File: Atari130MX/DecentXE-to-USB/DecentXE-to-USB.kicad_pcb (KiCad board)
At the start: 2 copper layers, 50.5 x 62.7 mm, 21 parts, among them J1 Conn_01x26, J2 Conn_01x09, Q1 Q_NPN_EBC, U1 Pico

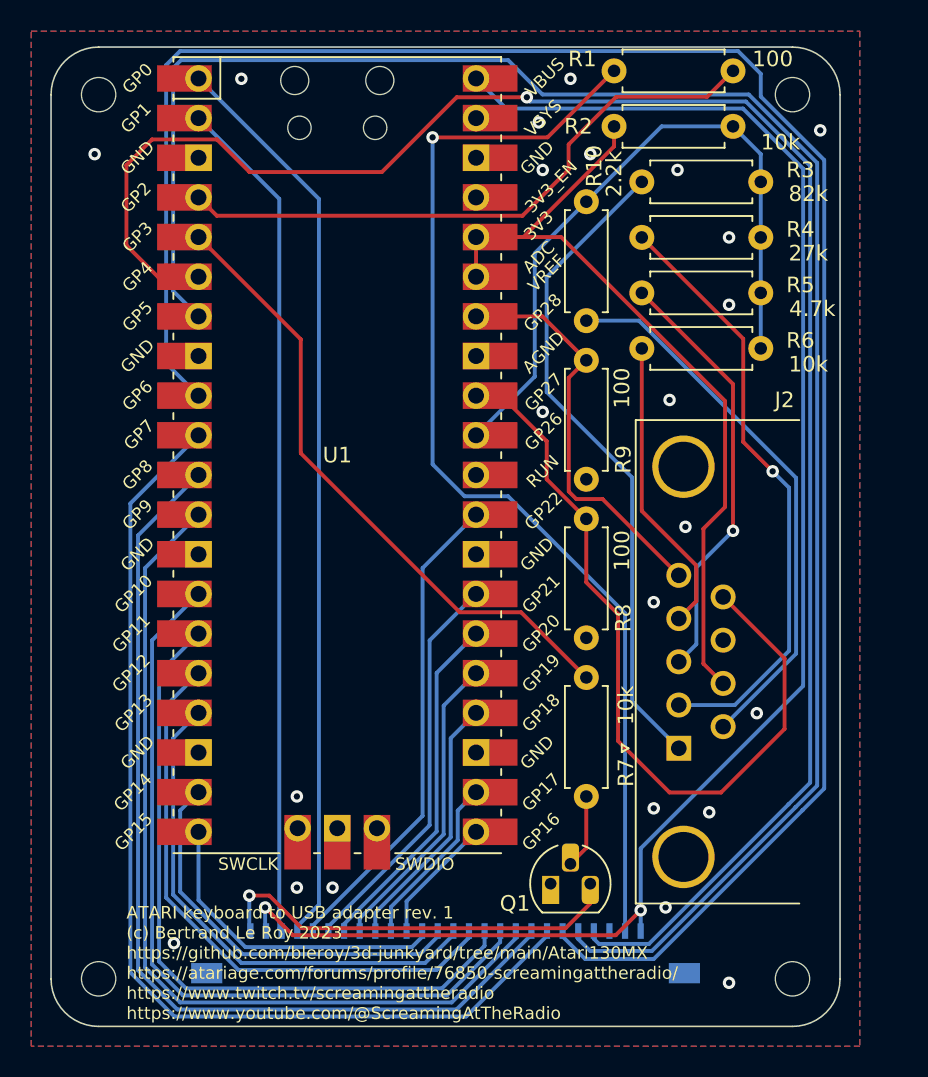
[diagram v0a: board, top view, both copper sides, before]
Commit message: Bettter design for the USB adapter
There will eventually be a 2040-based design that will do away with the Pico entirely. This is only a prototype.
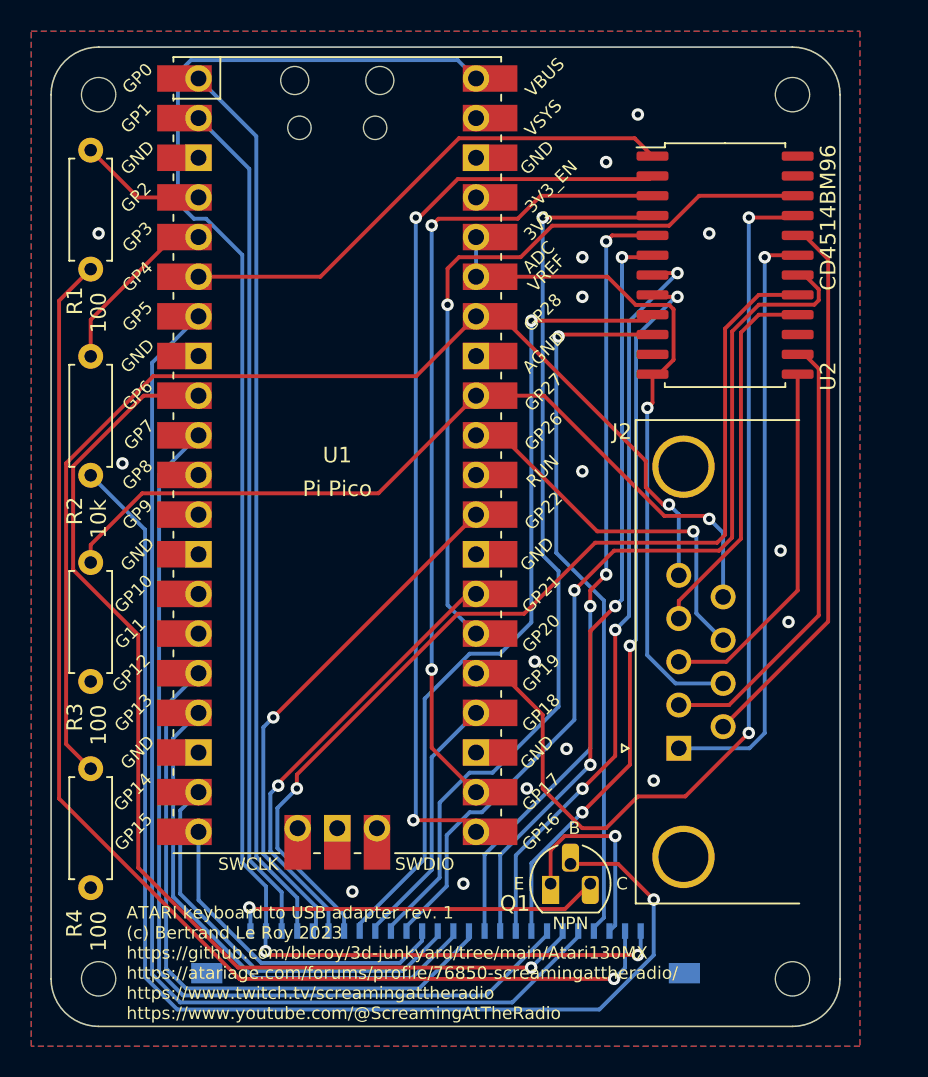
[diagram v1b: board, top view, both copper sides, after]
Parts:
- removed R10: 2.2k, Resistor_THT:R_Axial_DIN0207_L6.3mm_D2.5mm_P7.62mm_Horizontal
- removed R5: 4.7k, Resistor_THT:R_Axial_DIN0207_L6.3mm_D2.5mm_P7.62mm_Horizontal
- removed R6, R7: 10k, Resistor_THT:R_Axial_DIN0207_L6.3mm_D2.5mm_P7.62mm_Horizontal
- removed R8, R9: 100, Resistor_THT:R_Axial_DIN0207_L6.3mm_D2.5mm_P7.62mm_Horizontal
- removed REFe (x4): MountingHole_2.2mm_M2, MountingHole:MountingHole_2.2mm_M2
- added REF**: MountingHole_2.2mm_M2, MountingHole:MountingHole_2.2mm_M2, F.Cu at (15.7, 19.1)
- added REF**: MountingHole_2.2mm_M2, MountingHole:MountingHole_2.2mm_M2, F.Cu at (60.2, 19.1)
- added REF**: MountingHole_2.2mm_M2, MountingHole:MountingHole_2.2mm_M2, F.Cu at (60.2, 75.7)
- added REF**: MountingHole_2.2mm_M2, MountingHole:MountingHole_2.2mm_M2, F.Cu at (15.7, 75.7)
- added U2: CD4514BM96, Package_SO:SOIC-24W_7.5x15.4mm_P1.27mm, F.Cu at (55.9, 30.0)
- R3: value 82k -> 100
- R4: value 27k -> 100
- U1: value Pico -> Pi Pico
- moved R4 54.6 mm to (15.2, 69.8), turned to 90 degrees
- moved REF** 49.5 mm to (26.9, 29.5)
- moved R3 47.7 mm to (15.2, 56.6), turned to 90 degrees
- moved R2 40.3 mm to (15.2, 43.4), turned to 90 degrees
- moved R1 35.9 mm to (15.2, 30.2), turned to 90 degrees
- moved REF** 32.0 mm to (27.4, 40.1)
- moved G*** 2.29 mm to (27.6, 53.3)
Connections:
- J2 pad 8: GND -> JOY_GND
- R2 pad 1: 3V3 -> Net-(Q1-Pad2)
- R2 pad 2: Net-(U1-Pad31) -> Net-(R2-Pad2)
- R3 pad 1: UP -> GND
- R3 pad 2: Net-(U1-Pad31) -> PADDLE_A
- R4 pad 1: DOWN -> GND
- R4 pad 2: Net-(U1-Pad31) -> PADDLE_B
- U1 pad 11: COL_3 -> unconnected-(U1-Pad11)
- U1 pad 12: COL_4 -> unconnected-(U1-Pad12)
- U1 pad 14: COL_5 -> unconnected-(U1-Pad14)
- U1 pad 15: COL_6 -> unconnected-(U1-Pad15)
- U1 pad 21: COL_8 -> A0
- U1 pad 22: COL_7 -> A1
- U1 pad 25: COL_1 -> A2
- U1 pad 26: COL_9 -> A3
- U1 pad 31: Net-(U1-Pad31) -> JOY_GND
- U1 pad 5: Net-(R7-Pad2) -> Net-(R2-Pad2)
- U1 pad 6: COL_2 -> STROBE
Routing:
- net Net-(Q1-Pad2): track 4.74 -> 78.3 mm, vias 0 -> 1
- net COL_2: track 118.1 -> 45.5 mm
- net ROW_8: track 130.5 -> 68.0 mm, vias 0 -> 1
- net A2: track 0.00 -> 61.3 mm, vias 0 -> 2
- net A0: track 0.00 -> 59.3 mm, vias 0 -> 2
- net A1: track 0.00 -> 52.4 mm, vias 0 -> 2
- net COL_8: track 8.20 -> 59.5 mm, vias 0 -> 1
- net A3: track 0.00 -> 48.5 mm, vias 0 -> 1
- net ROW_7: track 121.2 -> 73.2 mm
- net COL_7: track 11.2 -> 58.0 mm, vias 0 -> 1
- net PADDLE_B: track 26.4 -> 71.9 mm, vias 0 -> 1
- net Net-(U1-Pad31): track 44.2 -> 0.00 mm
- net COL_9: track 22.6 -> 64.9 mm, vias 0 -> 1
- net Net-(R7-Pad2): track 40.8 -> 0.00 mm
- net STROBE: track 0.00 -> 33.2 mm
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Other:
- board text added: "B"
- board text added: "C"
- board text added: "E"
- board text added: "NPN"

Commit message: Fix the USB adapter
Decoder power supply was reversed. oops
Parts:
- U1: value Pi Pico -> Pico
- U2: value CD4514BM96 -> 4514
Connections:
- U2 pad 12: 3V3 -> GND
- U2 pad 24: GND -> 3V3
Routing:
- net 3V3: track 44.4 -> 61.6 mm, vias 1 -> 2

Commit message: USB adapter rev 2
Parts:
- removed Q1: Q_NPN_EBC, Package_TO_SOT_THT:TO-92_HandSolder
- removed R2: 10k, Resistor_THT:R_Axial_DIN0207_L6.3mm_D2.5mm_P7.62mm_Horizontal
- added R5: 100, Resistor_SMD:R_0603_1608Metric, B.Cu at (45.1, 50.2)
- added R6: 100, Resistor_SMD:R_0603_1608Metric, B.Cu at (45.1, 47.0)
- added R7: 100, Resistor_SMD:R_0603_1608Metric, B.Cu at (45.1, 40.6)
- added R8: 100, Resistor_SMD:R_0603_1608Metric, B.Cu at (45.1, 37.5)
- added R9: 100, Resistor_SMD:R_0603_1608Metric, B.Cu at (45.1, 43.8)
- G***, REF**: moved to F.Cu
- R1, R3, R4: footprint Resistor_THT:R_Axial_DIN0207_L6.3mm_D2.5mm_P7.62mm_Horizontal -> Resistor_SMD:R_0603_1608Metric; moved to B.Cu
- REF**: value OSHW-Logo2_7.3x6mm_SilkScreen -> OSHW-Logo2_7.3x6mm_Copper; footprint Symbol:OSHW-Logo2_7.3x6mm_SilkScreen -> Symbol:OSHW-Logo2_7.3x6mm_Copper; moved to F.Cu
- U2: moved to B.Cu
- moved R4 42.1 mm to (35.6, 33.0), turned to 0 degrees
- moved G*** 37.6 mm to (54.5, 27.0), turned to 0 degrees
- moved R3 37.3 mm to (45.1, 34.3), turned to -90 degrees
- moved REF** 34.3 mm to (54.9, 19.6), turned to 0 degrees
- moved R1 29.9 mm to (45.1, 31.1)
- moved U2 29.0 mm to (31.1, 45.1)
- moved REF** 29.0 mm to (55.1, 36.1), turned to 0 degrees
- moved J2 1.14 mm to (52.9, 62.1)
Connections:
- J1 pad 1: VCC_5V -> VCC_KBD
- J1 pad 25: VCC_5V -> VCC_LED
- J2 pad 7: 3V3 -> JOY_VCC
- U1 pad 11: unconnected-(U1-GPIO8-Pad11) -> JOY_VCC
- U1 pad 12: unconnected-(U1-GPIO9-Pad12) -> VCC_LED
- U1 pad 14: unconnected-(U1-GPIO10-Pad14) -> VCC_KBD
- U1 pad 40: VCC_5V -> unconnected-(U1-VBUS-Pad40)
- U1 pad 5: Net-(U1-GPIO3) -> LED_GND
- U2 pad 13: LEFT -> Net-(U2-Q13)
- U2 pad 14: DOWN -> Net-(U2-Q12)
- U2 pad 16: RIGHT -> Net-(U2-Q14)
- U2 pad 19: UP -> Net-(U2-Q11)
- U2 pad 20: FIRE -> Net-(U2-Q10)
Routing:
- net VCC_5V: track 104.5 -> 0.00 mm, vias 2 -> 0
- net JOY_VCC: track 0.00 -> 99.0 mm
- net Net-(Q1-B): track 78.3 -> 0.00 mm, vias 1 -> 0
- net VCC_KBD: track 0.00 -> 61.6 mm
- net A2: track 61.3 -> 11.9 mm, vias 2 -> 0
- net A3: track 48.5 -> 9.22 mm, vias 1 -> 0
- net VCC_LED: track 0.00 -> 37.3 mm, vias 0 -> 1
- net COL_2: track 45.5 -> 81.6 mm, vias 1 -> 2
- net 3V3: track 61.6 -> 26.8 mm, vias 2 -> 1
- net COL_9: track 64.9 -> 30.8 mm, vias 1 -> 0
- net ROW_7: track 73.2 -> 102.6 mm, vias 0 -> 1
- net COL_8: track 59.5 -> 30.4 mm, vias 1 -> 0
- net COL_7: track 58.0 -> 31.4 mm, vias 1 -> 2
- net PADDLE_B: track 71.9 -> 45.5 mm, vias 1 -> 0
- net A0: track 59.3 -> 32.9 mm
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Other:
- board text added: "ATARI keyboard to USB adapter rev. 2 (c) Bertrand Le Roy 2023 https://github.com/bleroy/3d-junkyard/tree/main/Atari130MX https://atariage.com/forums/profile/76850-screamingattheradio/ https://www.twitch.tv/screamingattheradio https://www.youtube.com/@ScreamingAtTheRadio"
- board text removed: "ATARI keyboard to USB adapter rev. 1 (c) Bertrand Le Roy 2023 https://github.com/bleroy/3d-junkyard/tree/main/Atari130MX https://atariage.com/forums/profile/76850-screamingattheradio/ https://www.twitch.tv/screamingattheradio https://www.youtube.com/@ScreamingAtTheRadio"
- board text removed: "B"
- board text removed: "C"
- board text removed: "E"
- board text removed: "NPN"

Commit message: USB Adapter rev. 3
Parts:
- removed R3, R4: 100, Resistor_SMD:R_0603_1608Metric
- added R2: 1k, Resistor_SMD:R_0603_1608Metric, B.Cu at (45.1, 34.3)
- REF**: value OSHW-Logo2_7.3x6mm_Copper -> OSHW-Logo2_7.3x6mm_SilkScreen; footprint Symbol:OSHW-Logo2_7.3x6mm_Copper -> Symbol:OSHW-Logo2_7.3x6mm_SilkScreen
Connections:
- J1 pad 25: VCC_LED -> 3V3
- U1 pad 12: VCC_LED -> unconnected-(U1-GPIO9-Pad12)
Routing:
- net 3V3: track 26.8 -> 98.3 mm, vias 1 -> 2
- net JOY_VCC: track 99.0 -> 45.8 mm
- net VCC_LED: track 37.3 -> 0.00 mm, vias 1 -> 0
- net COL_3: track 39.5 -> 74.8 mm
- net COL_2: track 81.6 -> 47.8 mm
- net COL_4: track 38.4 -> 70.1 mm
- net COL_5: track 37.1 -> 67.0 mm
- net COL_6: track 35.2 -> 64.1 mm
- net JOY_GND: track 23.4 -> 49.1 mm
- net ROW_7: track 102.6 -> 85.4 mm
- net ROW_8: track 91.8 -> 74.6 mm
- net PADDLE_B: track 45.5 -> 28.7 mm
- net ROW_5: track 45.9 -> 61.3 mm
- net SELECT: track 49.3 -> 34.4 mm, vias 1 -> 0
- net VCC_KBD: track 61.6 -> 47.3 mm, vias 0 -> 1
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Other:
- board text added: "+"
- board text added: "-"
- board text added: "ATARI keyboard to USB adapter rev. 3 (c) Bertrand Le Roy 2023 https://github.com/bleroy/3d-junkyard/tree/main/Atari130MX https://atariage.com/forums/profile/76850-screamingattheradio/ https://www.twitch.tv/screamingattheradio https://www.youtube.com/@ScreamingAtTheRadio"
- board text added: "FIRE"
- board text added: "LEFT"
- board text added: "PAD A"
- board text added: "PAD B"
- board text added: "RIGHT"
- board text added: "UP"
- board text removed: "ATARI keyboard to USB adapter rev. 2 (c) Bertrand Le Roy 2023 https://github.com/bleroy/3d-junkyard/tree/main/Atari130MX https://atariage.com/forums/profile/76850-screamingattheradio/ https://www.twitch.tv/screamingattheradio https://www.youtube.com/@ScreamingAtTheRadio"
